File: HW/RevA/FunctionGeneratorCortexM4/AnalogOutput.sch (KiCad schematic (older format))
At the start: 6 parts

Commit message: Finished Schema
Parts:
- removed U? (x5): TL074, symbol Amplifier_Operational:TL074
- added C15, C16, C21, C22: 100nF, Capacitor_SMD:C_1206_3216Metric_Pad1.42x1.75mm_HandSolder, symbol Device:C
- added C17, C18, C19, C20, C23, C24: 1nF, Capacitor_SMD:C_1206_3216Metric_Pad1.42x1.75mm_HandSolder, symbol Device:C
- added R10, R14, R15, R16, R17, R18, R19, R9: 1K, Resistor_SMD:R_1206_3216Metric_Pad1.42x1.75mm_HandSolder, symbol Device:R
- added R12, R13: 100R, Resistor_SMD:R_1206_3216Metric_Pad1.42x1.75mm_HandSolder, symbol Device:R
- added U12, U13: TL072, Package_SO:SOIC-8_3.9x4.9mm_P1.27mm, symbol Amplifier_Operational:TL072
- added U9: 74LVC1G3157, Package_TO_SOT_SMD:SC-70-8_Handsoldering, symbol 74xGxx:74LVC1G3157
- gave numbers to parts that had none: 1
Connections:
- net labels added: +5V, -5V, DCBIAS, DCBIAS_INVERT_IN, FUNC1_DCBIAS_IN, FUNC1_SIG_IN, FUNC1_SIG_OUT, FUNC1_SYNC_IN, FUNC1_SYNC_OUT, GNDS, SG0, SG0_IN, SG1, SG1_IN, SG2, SG2_IN
- net labels removed: AUX_IN, AUX_OUT, FUNC1_IN, FUNC1_OUT, FUNC2_IN, FUNC2_OUT
- wire segments 0 -> 118
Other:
- moved on the sheet: U11

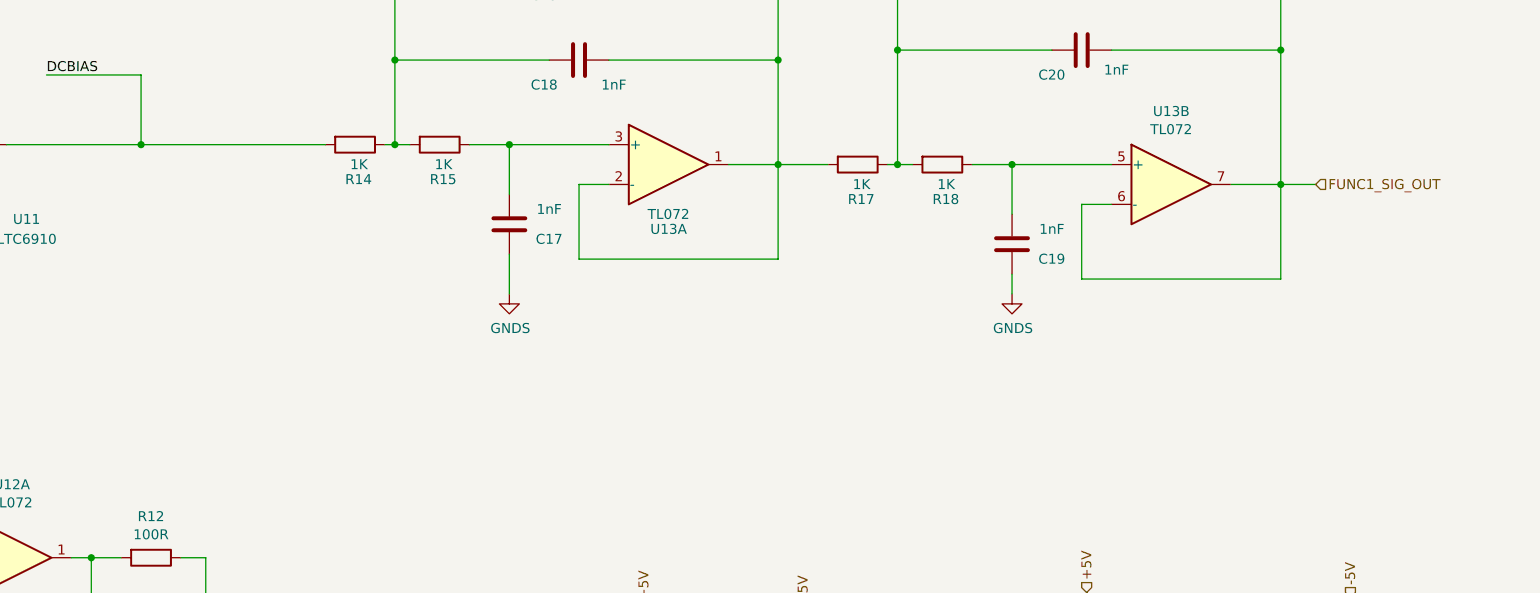
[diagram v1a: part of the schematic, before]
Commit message: hw update
Added bypass jumper for output filter
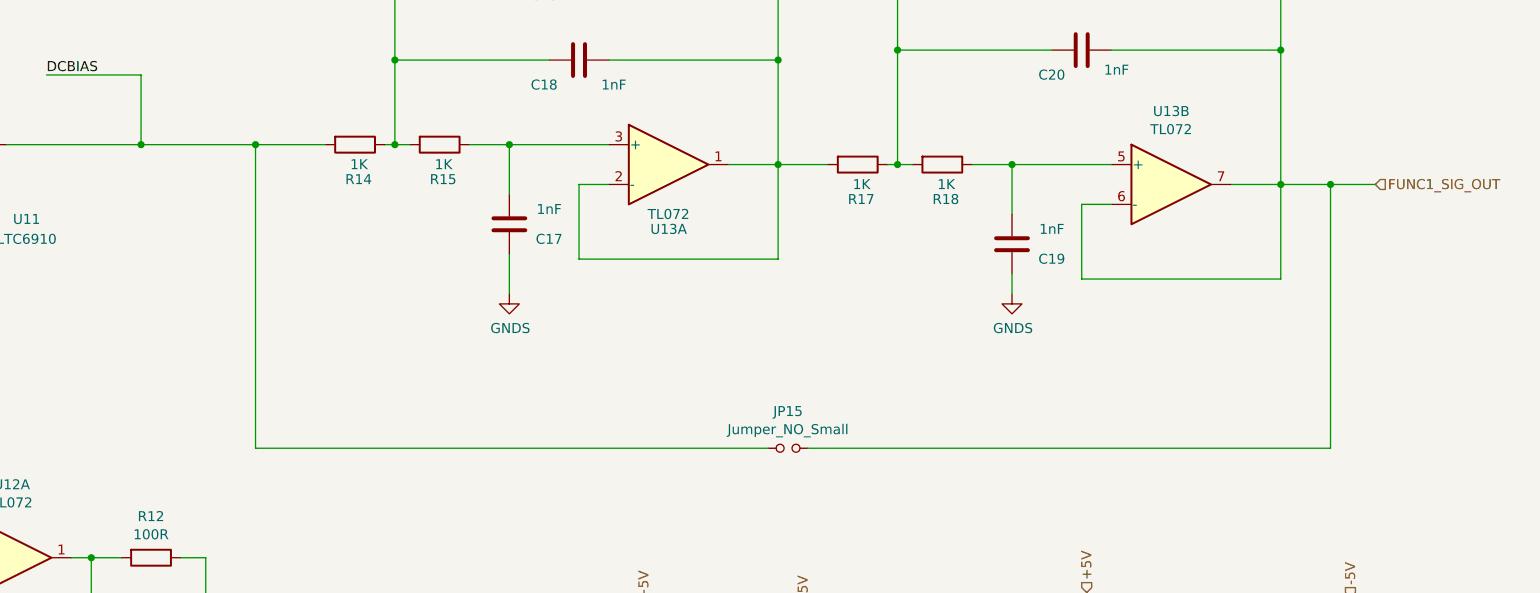
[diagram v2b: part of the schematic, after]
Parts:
- added JP15: Jumper_NO_Small, Jumper:SolderJumper-2_P1.3mm_Open_Pad1.0x1.5mm, symbol Device:Jumper_NO_Small
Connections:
- net DCBIAS: now also JP15.1
- net FUNC1_SIG_OUT: now also JP15.2
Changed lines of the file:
@@
 Wire Wire Line
 	4450 5225 4575 5225
-Text HLabel 10150 2150 2    50   Input ~ 0
+Text HLabel 10450 2150 2    50   Input ~ 0
 FUNC1_SIG_OUT
 Text Label 3775 1600 0    50   ~ 0
@@
 $EndComp
 Wire Wire Line
-	9975 2150 10150 2150
+	9975 2150 10225 2150
 Wire Wire Line
 	8975 2625 9975 2625
@@
 Connection ~ 4250 1950
 Wire Wire Line
-	4250 1950 5175 1950
+	4250 1950 4825 1950
 Connection ~ 8050 1475
 Wire Wire Line
@@
 Wire Wire Line
 	5525 1075 5525 1525
+$Comp
+L Device:Jumper_NO_Small JP15
+U 1 1 5ED419BB
+P 7500 3475
+F 0 "JP15" H 7500 3660 50  0000 C CNN
+F 1 "Jumper_NO_Small" H 7500 3569 50  0000 C CNN
+F 2 "Jumper:SolderJumper-2_P1.3mm_Open_Pad1.0x1.5mm" H 7500 3475 50  0001 C CNN
+F 3 "~" H 7500 3475 50  0001 C CNN
+	1    7500 3475
+	1    0    0    -1
+$EndComp
+Wire Wire Line
+	7400 3475 4825 3475
+Wire Wire Line
+	4825 3475 4825 1950
+Connection ~ 4825 1950
+Wire Wire Line
+	4825 1950 5175 1950
+Wire Wire Line
+	7600 3475 10225 3475
+Wire Wire Line
+	10225 3475 10225 2150
+Connection ~ 10225 2150
+Wire Wire Line
+	10225 2150 10450 2150
 $EndSCHEMATC

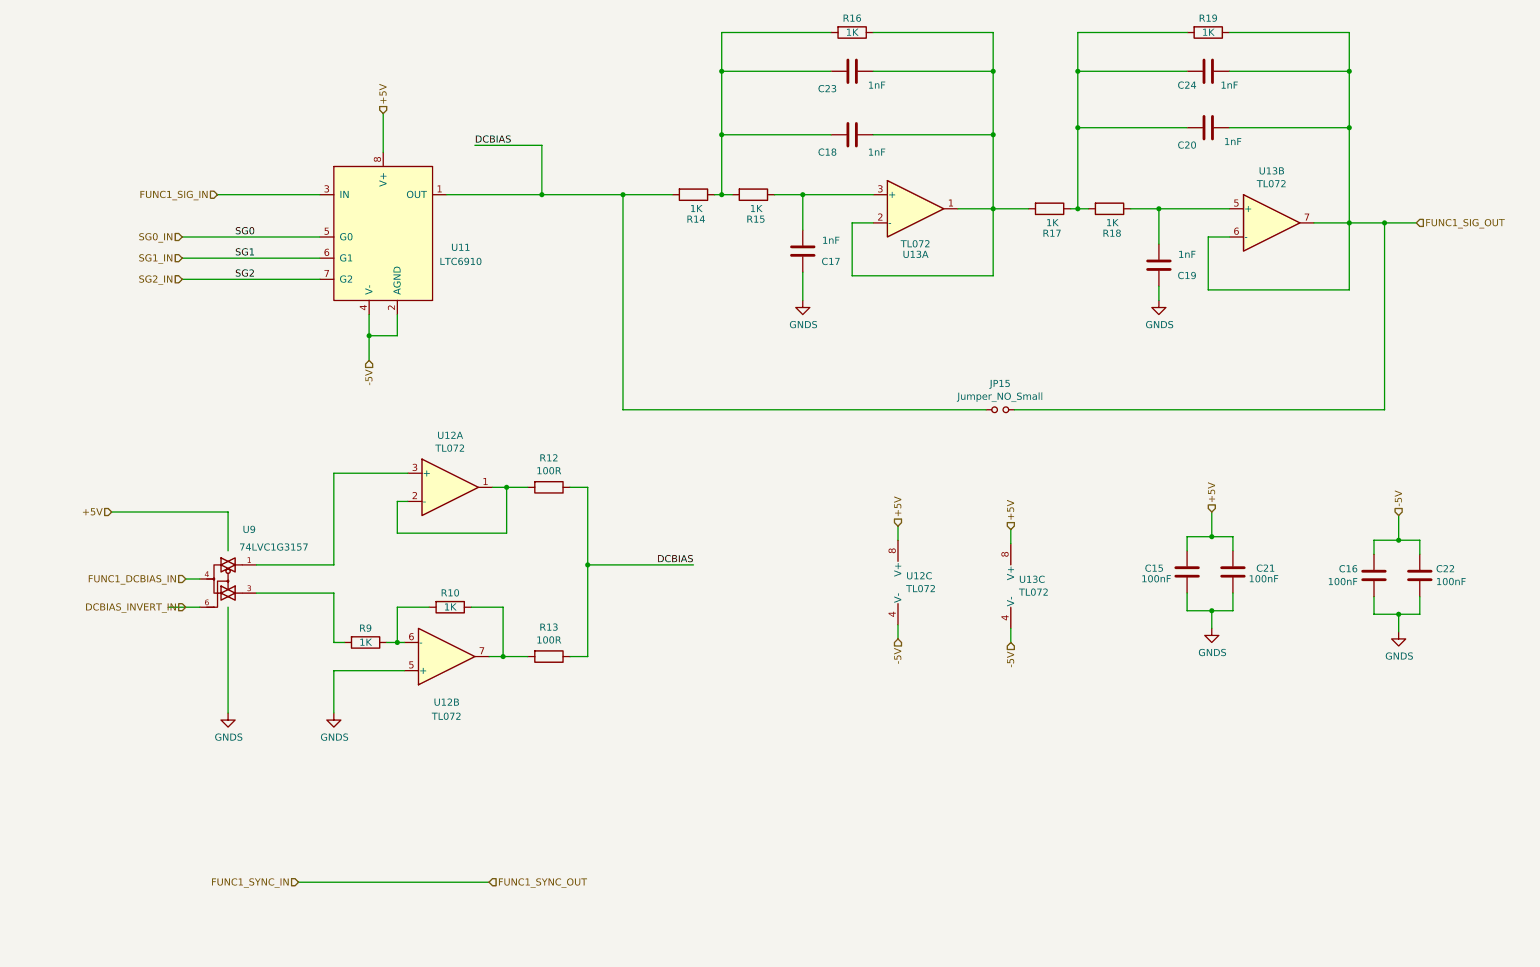
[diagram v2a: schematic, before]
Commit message: hw update
added passives to dc bias stage
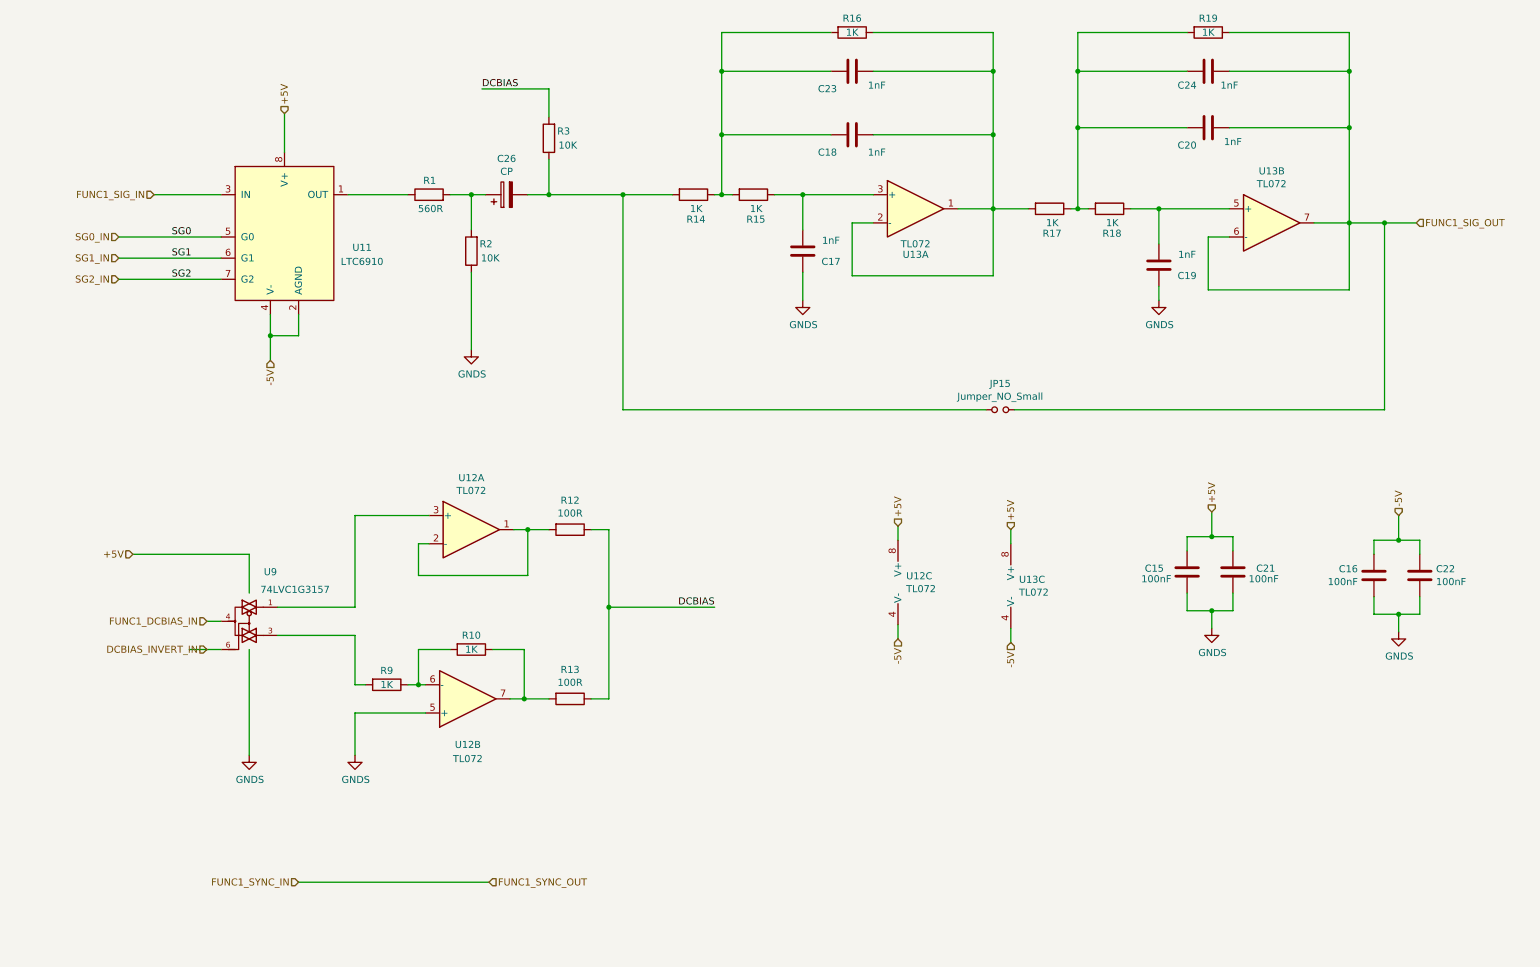
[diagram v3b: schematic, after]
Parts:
- added C26: CP, Capacitor_SMD:CP_Elec_4x5.7, symbol Device:CP
- added R1: 560R, Resistor_SMD:R_1206_3216Metric_Pad1.42x1.75mm_HandSolder, symbol Device:R
- added R2, R3: 10K, Resistor_SMD:R_1206_3216Metric_Pad1.42x1.75mm_HandSolder, symbol Device:R
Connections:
- net DCBIAS: now also R3.2; no longer JP15.1, R14.2, U11.1 (OUT)
- net GND: now also R2.1
- new net: C26.2, JP15.1, R14.2, R3.1
- new net: C26.1, R1.2, R2.2
- new net: R1.1, U11.1 (OUT)
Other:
- moved on the sheet: R10, R12, R13, R9, U11, U12A, U12B, U9

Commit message: Completed RevA layout
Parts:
- removed U9: 74LVC1G3157, Package_TO_SOT_SMD:SC-70-8_Handsoldering, symbol 74xGxx:74LVC1G3157
- added TP10, TP11, TP5, TP6, TP7, TP8, TP9: TestPoint, TestPoint:TestPoint_Pad_1.0x1.0mm, symbol Connector:TestPoint
- added U4: SN74LVC1G3157DCKR, Package_TO_SOT_SMD:SOT-363_SC-70-6_Handsoldering, symbol SN74LVC1G3157:SN74LVC1G3157DCKR
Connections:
- net DCBIAS: now also TP10.1
- net DCBIAS_INVERT_IN: now also TP6.1, U4.6 (S)
- net FUNC1_DCBIAS_IN: now also TP7.1, U4.4 (A)
- net FUNC1_SIG_IN: now also TP5.1
- net FUNC1_SIG_OUT: now also TP11.1
- net at C26.2, JP15.1, R14.2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: now also TP9.1
- net at R1.1, U11.1 (OUT): now also TP8.1
- net at U12.3 (+): now also U4.3 (B1)
- net at R9.2: now also U4.1 (B2)
- net GND renamed GNDS
- net GNDS: now also U4.2 (GND)
- net VCC renamed +5V
- net +5V: now also U4.5 (VCC)
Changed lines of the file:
@@
 Text HLabel 1500 1950 0    50   Input ~ 0
 FUNC1_SIG_IN
-Text HLabel 1875 4975 0    50   Input ~ 0
+Text HLabel 1650 5125 0    50   Input ~ 0
 FUNC1_DCBIAS_IN
 Text HLabel 3875 6825 2    50   Input ~ 0
@@
 	1    0    0    -1
 $EndComp
-$Comp
-L 74xGxx:74LVC1G3157 U9
-U 1 1 5E61EF05
-P 2175 4975
-F 0 "U9" H 2325 5325 50  0000 C CNN
-F 1 "74LVC1G3157" H 2500 5200 50  0000 C CNN
-F 2 "Package_TO_SOT_SMD:SC-70-8_Handsoldering" H 2175 4975 50  0001 C CNN
-F 3 "http://www.ti.com/lit/ds/symlink/sn74lvc1g3157.pdf" H 2175 4975 50  0001 C CNN
-	1    2175 4975
-	1    0    0    -1
-$EndComp
-Wire Wire Line
-	1875 4975 1975 4975
-Wire Wire Line
-	2175 5175 2175 5925
+Wire Wire Line
+	1650 4925 1775 4925
 $Comp
 L power:GNDS #PWR0126
@@
 	1    0    0    -1
 $EndComp
-Text HLabel 1350 4500 0    50   Input ~ 0
-+5V
-Wire Wire Line
-	1350 4500 2175 4500
-Wire Wire Line
-	2175 4500 2175 4775
-Wire Wire Line
-	1975 5175 1750 5175
-Text HLabel 1875 5175 0    50   Input ~ 0
+Wire Wire Line
+	2175 4500 2175 4725
+Wire Wire Line
+	1875 5125 1775 5125
+Text HLabel 1650 4925 0    50   Input ~ 0
 DCBIAS_INVERT_IN
 $Comp
@@
 	3000 5425 2925 5425
 Wire Wire Line
-	2925 5425 2925 5075
-Wire Wire Line
-	2925 5075 2375 5075
+	2925 5425 2925 5125
+Wire Wire Line
+	2925 5125 2475 5125
 Wire Wire Line
 	3375 5425 3375 5175
@@
 	3900 5175 4125 5175
 Wire Wire Line
-	2375 4875 2925 4875
-Wire Wire Line
-	2925 4875 2925 4225
+	2475 4925 2925 4925
+Wire Wire Line
+	2925 4925 2925 4225
 Wire Wire Line
 	2925 4225 3450 4225
@@
 	4150 4325 4300 4325
 Wire Wire Line
-	4725 4875 5475 4875
+	4725 4875 5000 4875
 Connection ~ 4725 4875
 Wire Wire Line
@@
 DCBIAS
 Wire Wire Line
-	1975 1950 1500 1950
+	1975 1950 1625 1950
 Text HLabel 2425 1375 1    50   Input ~ 0
 +5V
@@
 	3825 1200 4300 1200
 Wire Wire Line
-	2875 1950 3300 1950
+	2875 1950 3050 1950
 $Comp
 L Amplifier_Operational:TL072 U12
@@
 Wire Wire Line
 	3600 1950 3750 1950
+Wire Wire Line
+	2175 5325 2175 5925
+$Comp
+L SN74LVC1G3157:SN74LVC1G3157DCKR U4
+U 1 1 5E6AFCB0
+P 2175 5025
+F 0 "U4" H 1475 5525 50  0000 C CNN
+F 1 "SN74LVC1G3157DCKR" H 1275 5400 50  0000 C CNN
+F 2 "Package_TO_SOT_SMD:SOT-363_SC-70-6_Handsoldering" H 1975 4725 50  0001 C CNN
+F 3 "http://www.ti.com/lit/ds/symlink/sn74lvc1g3157.pdf" H 2275 5225 50  0001 C CNN
+	1    2175 5025
+	1    0    0    -1
+$EndComp
+Text HLabel 2175 4500 1    50   Input ~ 0
++5V
+$Comp
+L Connector:TestPoint TP?
+U 1 1 5E6322DB
+P 1625 1800
+AR Path="/5E5FDE87/5E6322DB" Ref="TP?"  Part="1"
+AR Path="/5EBB9B06/5E6322DB" Ref="TP5"  Part="1"
+F 0 "TP5" H 1683 1872 50  0000 L CNN
+F 1 "TestPoint" H 1683 1827 50  0001 L CNN
+F 2 "TestPoint:TestPoint_Pad_1.0x1.0mm" H 1825 1800 50  0001 C CNN
+F 3 "~" H 1825 1800 50  0001 C CNN
+	1    1625 1800
+	1    0    0    -1
+$EndComp
+Wire Wire Line
+	1625 1800 1625 1950
+Connection ~ 1625 1950
+Wire Wire Line
+	1625 1950 1500 1950
+$Comp
+L Connector:TestPoint TP?
+U 1 1 5E6371FD
+P 1775 5275
+AR Path="/5E5FDE87/5E6371FD" Ref="TP?"  Part="1"
+AR Path="/5EBB9B06/5E6371FD" Ref="TP7"  Part="1"
+F 0 "TP7" H 1833 5347 50  0000 L CNN
+F 1 "TestPoint" H 1833 5302 50  0001 L CNN
+F 2 "TestPoint:TestPoint_Pad_1.0x1.0mm" H 1975 5275 50  0001 C CNN
+F 3 "~" H 1975 5275 50  0001 C CNN
+	1    1775 5275
+	-1   0    0    1
+$EndComp
+Wire Wire Line
+	1775 5275 1775 5125
+Connection ~ 1775 5125
+Wire Wire Line
+	1775 5125 1650 5125
+$Comp
+L Connector:TestPoint TP?
+U 1 1 5E63C5E2
+P 1775 4775
+AR Path="/5E5FDE87/5E63C5E2" Ref="TP?"  Part="1"
+AR Path="/5EBB9B06/5E63C5E2" Ref="TP6"  Part="1"
+F 0 "TP6" H 1833 4847 50  0000 L CNN
+F 1 "TestPoint" H 1833 4802 50  0001 L CNN
+F 2 "TestPoint:TestPoint_Pad_1.0x1.0mm" H 1975 4775 50  0001 C CNN
+F 3 "~" H 1975 4775 50  0001 C CNN
+	1    1775 4775
+	1    0    0    -1
+$EndComp
+Wire Wire Line
+	1775 4775 1775 4925
+Connection ~ 1775 4925
+Wire Wire Line
+	1775 4925 1875 4925
+$Comp
+L Connector:TestPoint TP?
+U 1 1 5E641AB5
+P 5000 4725
+AR Path="/5E5FDE87/5E641AB5" Ref="TP?"  Part="1"
+AR Path="/5EBB9B06/5E641AB5" Ref="TP10"  Part="1"
+F 0 "TP10" H 5058 4797 50  0000 L CNN
+F 1 "TestPoint" H 5058 4752 50  0001 L CNN
+F 2 "TestPoint:TestPoint_Pad_1.0x1.0mm" H 5200 4725 50  0001 C CNN
+F 3 "~" H 5200 4725 50  0001 C CNN
+	1    5000 4725
+	1    0    0    -1
+$EndComp
+Wire Wire Line
+	5000 4725 5000 4875
+Connection ~ 5000 4875
+Wire Wire Line
+	5000 4875 5475 4875
+$Comp
+L Connector:TestPoint TP?
+U 1 1 5E64776B
+P 3050 1800
+AR Path="/5E5FDE87/5E64776B" Ref="TP?"  Part="1"
+AR Path="/5EBB9B06/5E64776B" Ref="TP8"  Part="1"
+F 0 "TP8" H 3108 1872 50  0000 L CNN
+F 1 "TestPoint" H 3108 1827 50  0001 L CNN
+F 2 "TestPoint:TestPoint_Pad_1.0x1.0mm" H 3250 1800 50  0001 C CNN
+F 3 "~" H 3250 1800 50  0001 C CNN
+	1    3050 1800
+	1    0    0    -1
+$EndComp
+Wire Wire Line
+	3050 1800 3050 1950
+Connection ~ 3050 1950
+Wire Wire Line
+	3050 1950 3300 1950
+$Comp
+L Connector:TestPoint TP?
+U 1 1 5E64CF74
+P 4825 1800
+AR Path="/5E5FDE87/5E64CF74" Ref="TP?"  Part="1"
+AR Path="/5EBB9B06/5E64CF74" Ref="TP9"  Part="1"
+F 0 "TP9" H 4883 1872 50  0000 L CNN
+F 1 "TestPoint" H 4883 1827 50  0001 L CNN
+F 2 "TestPoint:TestPoint_Pad_1.0x1.0mm" H 5025 1800 50  0001 C CNN
+F 3 "~" H 5025 1800 50  0001 C CNN
+	1    4825 1800
+	1    0    0    -1
+$EndComp
+Wire Wire Line
+	4825 1800 4825 1950
+$Comp
+L Connector:TestPoint TP?
+U 1 1 5E652412
+P 10225 2000
+AR Path="/5E5FDE87/5E652412" Ref="TP?"  Part="1"
+AR Path="/5EBB9B06/5E652412" Ref="TP11"  Part="1"
+F 0 "TP11" H 10283 2072 50  0000 L CNN
+F 1 "TestPoint" H 10283 2027 50  0001 L CNN
+F 2 "TestPoint:TestPoint_Pad_1.0x1.0mm" H 10425 2000 50  0001 C CNN
+F 3 "~" H 10425 2000 50  0001 C CNN
+	1    10225 2000
+	1    0    0    -1
+$EndComp
+Wire Wire Line
+	10225 2000 10225 2150
 $EndSCHEMATC
